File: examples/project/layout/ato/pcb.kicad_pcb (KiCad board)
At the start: 2 copper layers, 2 parts

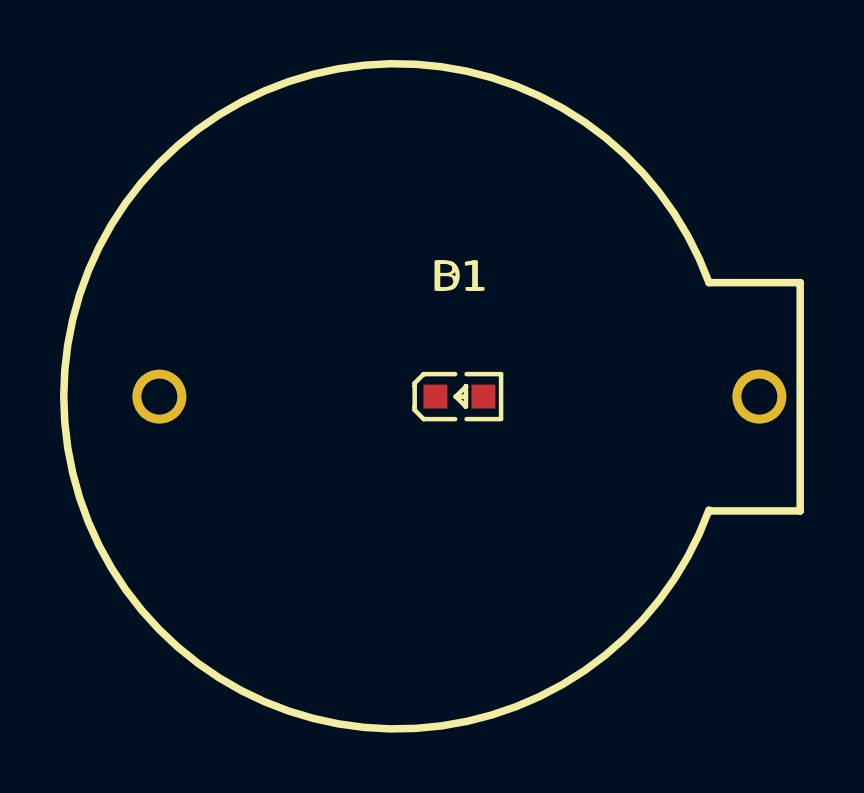
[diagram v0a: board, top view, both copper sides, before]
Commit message: `ato` -> PCB (#582)
Compile ato code to a PCB through the common `buildutil`-based pipeline
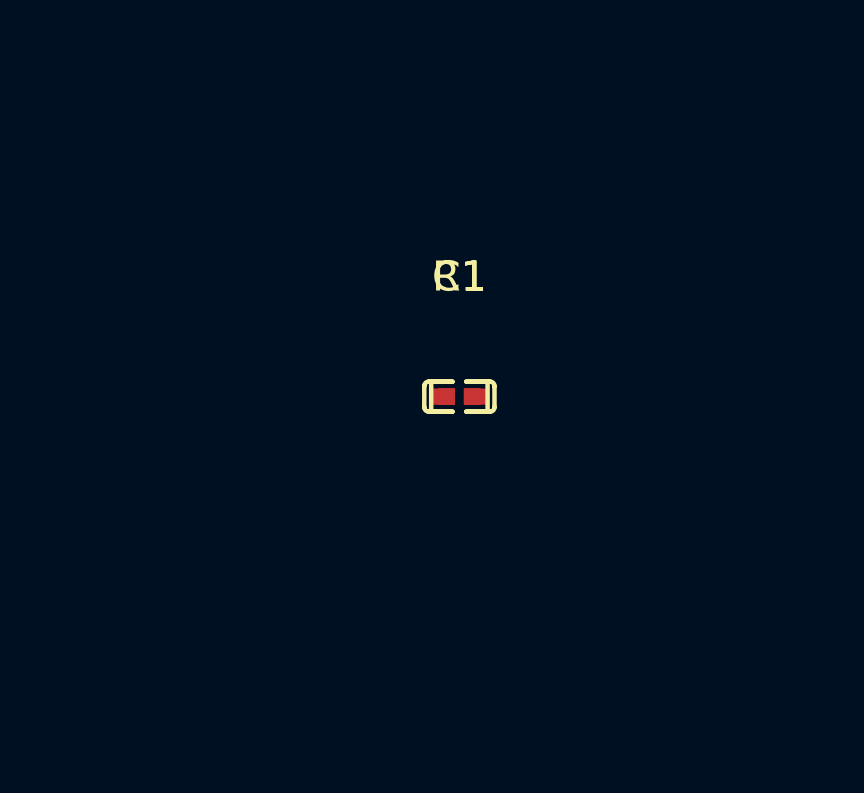
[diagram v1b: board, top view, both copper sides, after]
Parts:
- removed B1: Battery, lcsc:BAT-TH_BS-02-A1AJ010
- removed D1: PoweredLED, lcsc:LED0603-RD-YELLOW
- added C1: 100nF ±10% 16V X7R, lcsc:C0402, F.Cu at (0.00, 0.00)
- added R1: 10kΩ ±1% 62.5mW, lcsc:R0402, F.Cu at (0.00, 0.00)
